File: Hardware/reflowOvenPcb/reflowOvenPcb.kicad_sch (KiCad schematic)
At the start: 27 parts, among them J1 ISP, J2 Fan_output, J4 SSR_Output, Q1 2N3904, Q2 2N3904, Q3 2N3904, SW1 SW_RST, U1 ATmega328-M, U2 DM-OLED096-636, Y1 8MHz

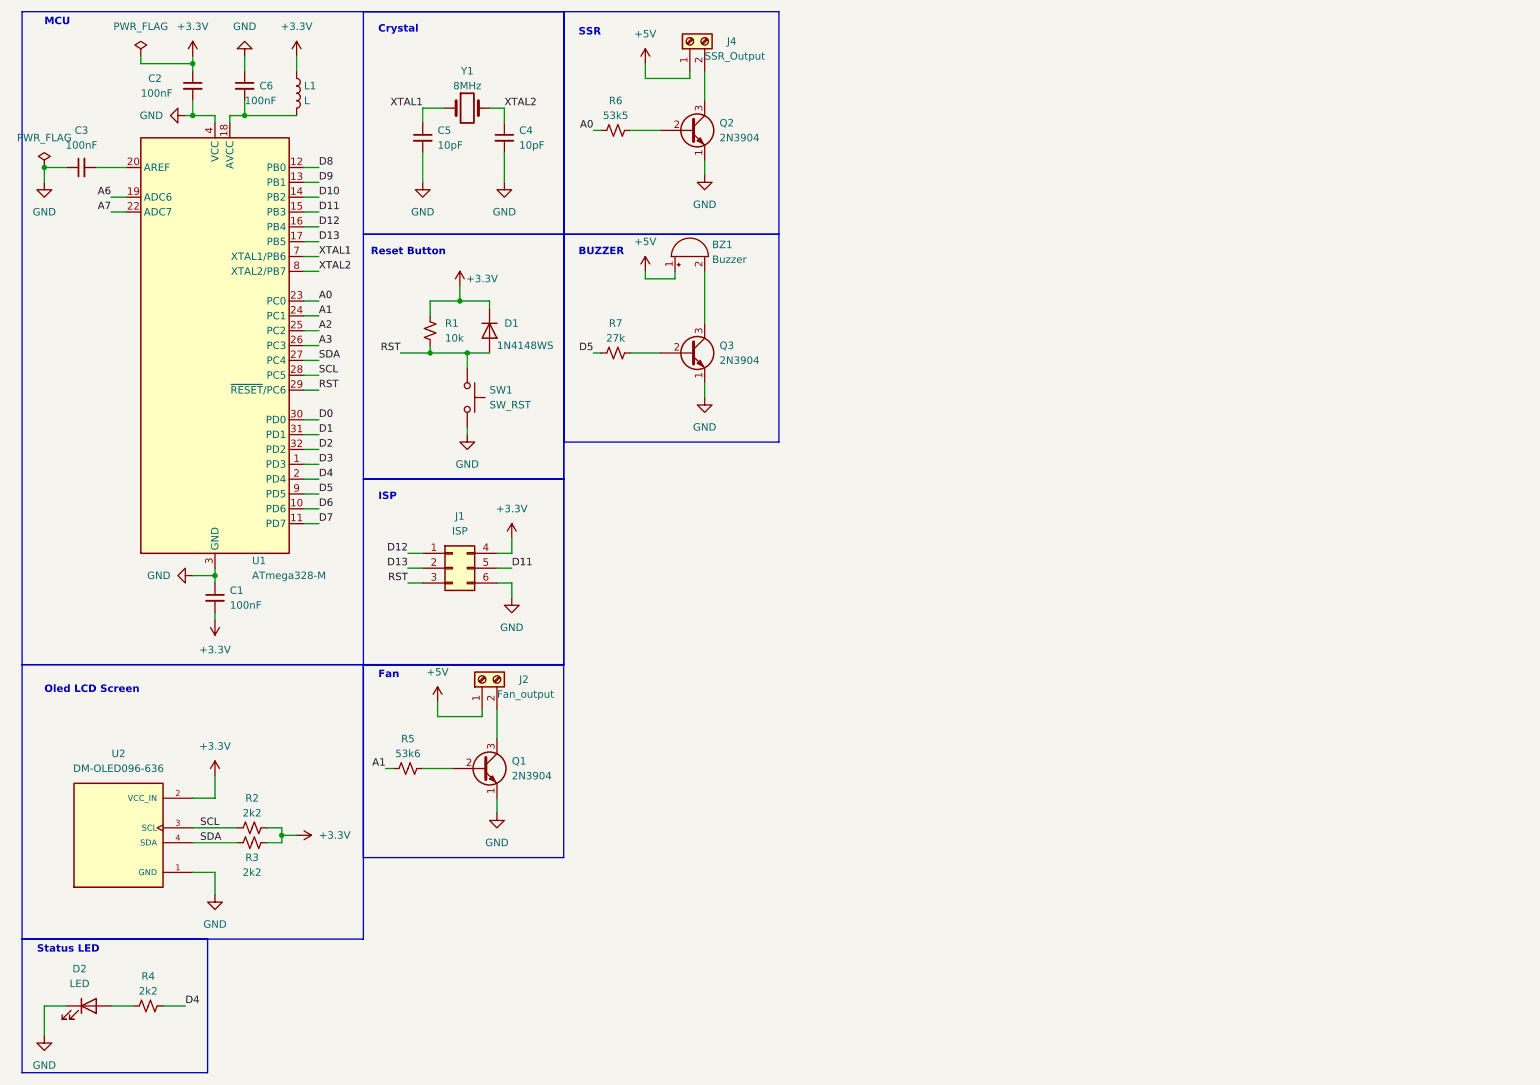
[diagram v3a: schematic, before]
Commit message: Added multiple libraris, and place all the components
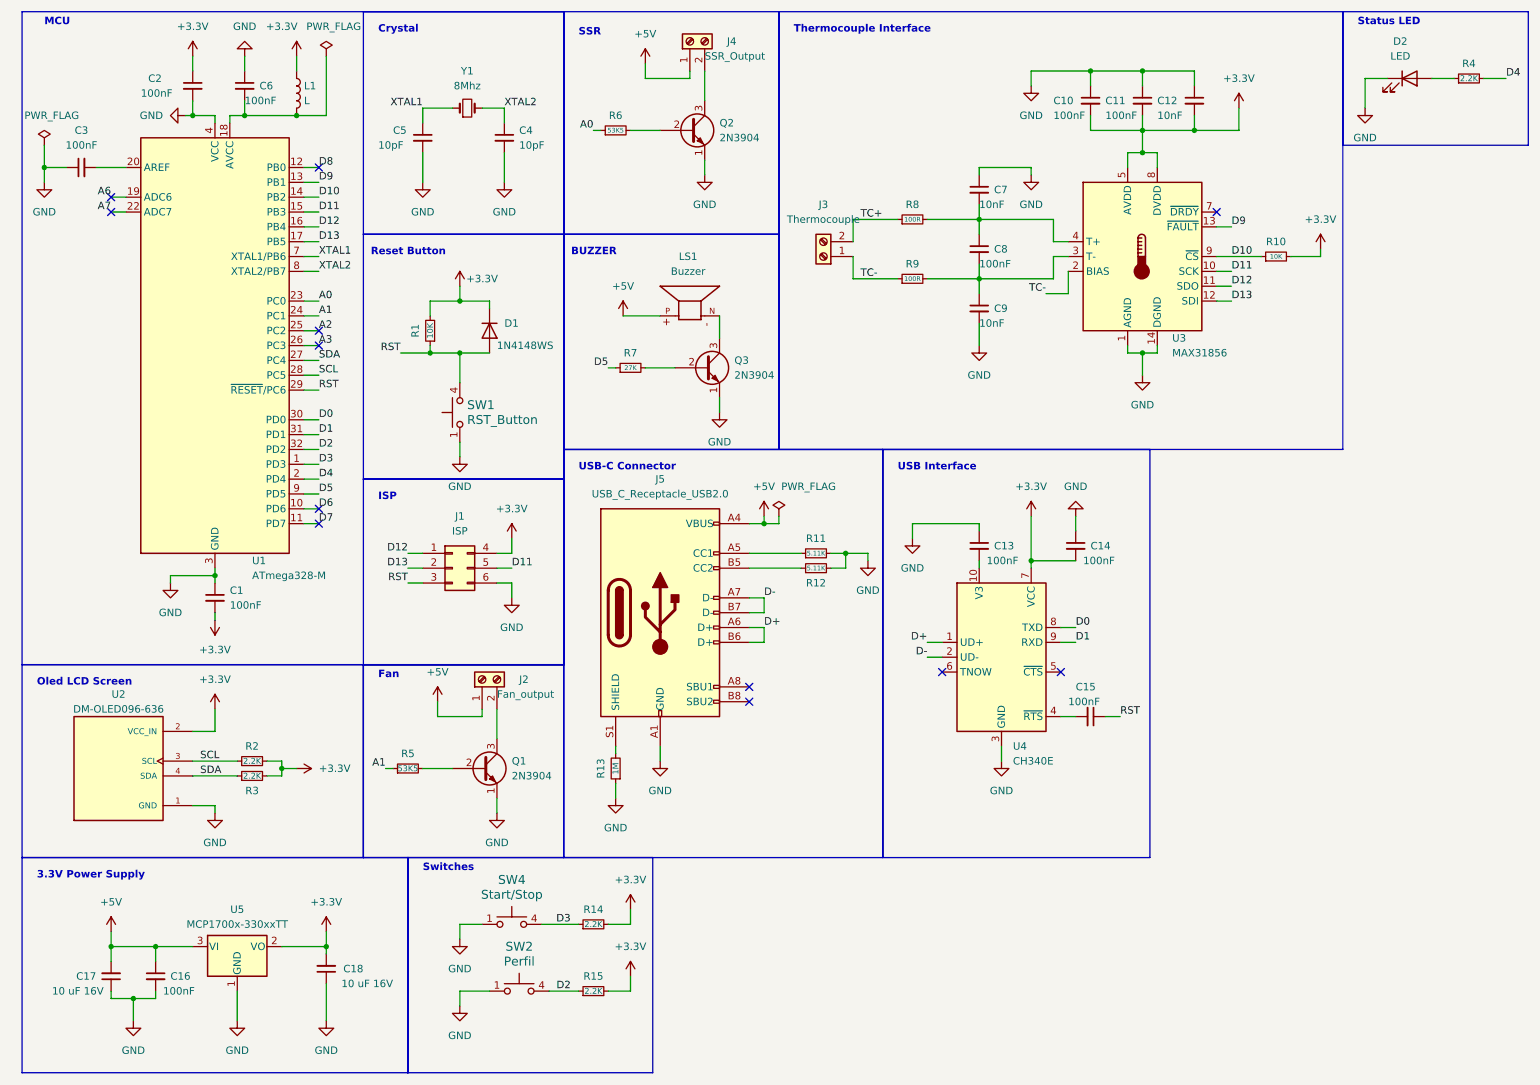
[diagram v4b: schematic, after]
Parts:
- removed BZ1: Buzzer, symbol Device:Buzzer
- removed R1: 10k, symbol Device:R_Small_US
- removed R2, R3, R4: 2k2, symbol Device:R_Small_US
- removed R5: 53k6, symbol Device:R_Small_US
- removed R6: 53k5, symbol Device:R_Small_US
- removed R7: 27k, symbol Device:R_Small_US
- removed SW1: SW_RST, symbol Switch:SW_Push
- removed U2: DM-OLED096-636, OLED_SSD1306:MODULE_DM-OLED096-636, symbol OLED_SSD1306:DM-OLED096-636
- removed Y1: 8MHz, symbol Device:Crystal
- added C10, C11, C13, C14, C15, C16, C8: 100nF, Capacitor_SMD:C_0805_2012Metric, symbol Device:C_Small
- added C12, C7, C9: 10nF, Capacitor_SMD:C_0805_2012Metric, symbol Device:C_Small
- added C17, C18: 10 uF 16V, Capacitor_SMD:C_0805_2012Metric, symbol Device:C_Small
- added J3: Thermocouple, TerminalBlock_Phoenix:TerminalBlock_Phoenix_PT-1,5-2-5.0-H_1x02_P5.00mm_Horizontal, symbol Connector:Screw_Terminal_01x02
- added J5: USB_C_Receptacle_USB2.0, Connector_USB:USB_C_Receptacle_GCT_USB4105-xx-A_16P_TopMnt_Horizontal, symbol Connector:USB_C_Receptacle_USB2.0
- added LS1: Buzzer, Buzzer_SMD:CUI_CMI-9705-0580-SMT-TR, symbol Buzzer_SMD:CMI-9705-0580-SMT-TR
- added R1, R10: 10K, Resistor_SMD:R_0805_2012Metric, symbol Device:R_Small
- added R11, R12: 5.11K, Resistor_SMD:R_0805_2012Metric, symbol Device:R_Small
- added R13: 1M, Resistor_SMD:R_0805_2012Metric, symbol Device:R_Small
- added R14, R15, R2, R3, R4: 2.2K, Resistor_SMD:R_0805_2012Metric, symbol Device:R_Small
- added R5, R6: 53K5, Resistor_SMD:R_0805_2012Metric, symbol Device:R_Small
- added R7: 27K, Resistor_SMD:R_0805_2012Metric, symbol Device:R_Small
- added R8, R9: 100R, Resistor_SMD:R_0805_2012Metric, symbol Device:R_Small
- added SW1: RST_Button, SPST_Button_SMD:SW4_PTS815 SJM 250 SMTR LFS_CNK, symbol SW_SPST:PTS815_SJM_250_SMTR_LFS
- added SW2: Perfil, SPST_Button_SMD:SW4_PTS815 SJM 250 SMTR LFS_CNK, symbol SW_SPST:PTS815_SJM_250_SMTR_LFS
- added SW4: Start/Stop, SPST_Button_SMD:SW4_PTS815 SJM 250 SMTR LFS_CNK, symbol SW_SPST:PTS815_SJM_250_SMTR_LFS
- added U2: DM-OLED096-636, Oled_096:MODULE_DM-OLED096-636, symbol OLED_091:DM-OLED096-636
- added U3: MAX31856, Package_SO:TSSOP-14_4.4x5mm_P0.65mm, symbol Sensor_Temperature:MAX31856
- added U4: CH340E, Package_SO:MSOP-10_3x3mm_P0.5mm, symbol Interface_USB:CH340E
- added U5: MCP1700x-330xxTT, Package_TO_SOT_SMD:SOT-23, symbol Regulator_Linear:MCP1700x-330xxTT
- added Y1: 8Mhz, Crystal:Crystal_SMD_5032-2Pin_5.0x3.2mm, symbol Device:Crystal_Small
- C1, C2, C3, C4, C5, C6: footprint (none) -> Capacitor_SMD:C_0805_2012Metric
- D2: footprint (none) -> LED_SMD:LED_0805_2012Metric
- J1: footprint Connector_PinHeader_1.00mm:PinHeader_2x03_P1.00mm_Vertical_SMD -> Connector_PinHeader_2.54mm:PinHeader_2x03_P2.54mm_Vertical_SMD
- J2, J4: footprint (none) -> TerminalBlock_Phoenix:TerminalBlock_Phoenix_PT-1,5-2-5.0-H_1x02_P5.00mm_Horizontal
- L1: footprint (none) -> Inductor_SMD:L_0805_2012Metric
- Q1, Q2, Q3: footprint Package_TO_SOT_THT:TO-92_Inline -> Package_TO_SOT_SMD:SOT-89-3
- U1: footprint Package_DFN_QFN:QFN-32-1EP_5x5mm_P0.5mm_EP3.1x3.1mm -> Package_QFP:TQFP-32_7x7mm_P0.8mm
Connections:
- net +3.3V: now also C10.2, C11.2, C12.2, C14.2, C18.2, R1.2, R10.2, R14.2, R15.2, R2.2, R3.2, U2.2 (VCC_IN), U3.5 (AVDD), U3.8 (DVDD), U4.7 (VCC), U5.2 (VO)
- net +5V: now also C16.1, C17.2, J5.A4 (VBUS), J5.A9 (VBUS), J5.B4 (VBUS), J5.B9 (VBUS), LS1.P, U5.3 (VI)
- net A0: now also R6.1
- net A1: now also R5.1
- net D0: now also U4.8 (TXD)
- net D1: now also U4.9 (RXD)
- net D10: now also R10.1, U3.9 (~{CS})
- net D11: now also U3.10 (SCK)
- net D12: now also U3.11 (SDO)
- net D13: now also U3.12 (SDI)
- net D2: now also R15.1, SW2.4
- net D3: now also R14.1, SW4.4
- net D4: now also R4.2
- net D5: now also R7.1
- net D9: now also U3.13 (~{FAULT})
- net GND: now also C10.1, C11.1, C12.1, C13.1, C14.1, C16.2, C17.1, C18.1, C7.1, C9.2, J5.A1 (GND), J5.A12 (GND), J5.B1 (GND), J5.B12 (GND), R11.2, R12.2, R13.1, SW1.1, SW2.1, SW4.1, U2.1 (GND), U3.1 (AGND), U3.14 (DGND), U4.3 (GND), U5.1 (GND)
- net RST: now also C15.1, R1.1, SW1.4
- net SCL: now also R2.1, U2.3 (SCL)
- net SDA: now also R3.1, U2.4 (SDA)
- net XTAL1: now also Y1.1
- net XTAL2: now also Y1.2
- net at Q2.2 (B): now also R6.2
- net at Q1.2 (B): now also R5.2
- net at D2.2 (A): now also R4.1
- net at Q3.2 (B): now also R7.2
- net at Q3.3 (C): now also LS1.N
- new net: C15.2, U4.4 (~{RTS})
- new net: C13.2, U4.10 (V3)
- new net: C7.2, C8.1, R8.2, U3.4 (T+)
- new net: C8.2, C9.1, R9.2, U3.3 (T-)
- new net: J5.A5 (CC1), R11.1
- new net: J5.B5 (CC2), R12.1
- new net: J5.S1 (SHIELD), R13.2
- new net D+: J5.A6 (D+), J5.B6 (D+), U4.1 (UD+)
- new net D-: J5.A7 (D-), J5.B7 (D-), U4.2 (UD-)
- new net TC+: J3.2 (Pin_2), R8.1
- new net TC-: J3.1 (Pin_1), R9.1, U3.2 (BIAS)
- no-connect marks 0 -> 12
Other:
- note added: "3.3V Power Supply"
- note added: "Switches"
- note added: "Thermocouple Interface"
- note added: "USB Interface"
- note added: "USB-C Connector"
- moved on the sheet: D2, Q3
